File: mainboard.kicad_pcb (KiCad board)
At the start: 2 copper layers, 76.8 x 33.7 mm, 38 parts, among them J1 105017-1001, J2 Conn_01x04_Female, J3 Conn_01x02_Female, J4 Conn_01x09_Female, J5 Conn_01x02_Female, J6 Conn_01x02_Female, J7 Conn_01x04_Female, J8 Conn_01x03_Female, Q1 AOD4184A, U1 ESP32-WROOM-32E_(16MB)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

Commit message: h
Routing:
- net IRB: track 28.8 -> 30.6 mm
- net 3V3: track 129.9 -> 130.5 mm
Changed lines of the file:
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@@
-(kicad_pcb (version 20171130) (host pcbnew "(5.1.9)-1")
+(kicad_pcb (version 20171130) (host pcbnew "(5.1.9-0-10_14)")
   (general
     (thickness 1.6)
-    (drawings 29)
-    (tracks 313)
+    (drawings 31)
+    (tracks 316)
     (zones 0)
     (modules 38)
@@
   )
   (setup
-    (last_trace_width 0.25)
+    (last_trace_width 0.635)
     (user_trace_width 0.4)
     (user_trace_width 0.5)
@@
     )
   )
+  (dimension 33.655 (width 0.15) (layer Dwgs.User)
+    (gr_text "33.655 mm" (at 156.24 99.3775 90) (layer Dwgs.User)
+      (effects (font (size 1 1) (thickness 0.15)))
+    )
+    (feature1 (pts (xy 147.955 82.55) (xy 155.526421 82.55)))
+    (feature2 (pts (xy 147.955 116.205) (xy 155.526421 116.205)))
+    (crossbar (pts (xy 154.94 116.205) (xy 154.94 82.55)))
+    (arrow1a (pts (xy 154.94 82.55) (xy 155.526421 83.676504)))
+    (arrow1b (pts (xy 154.94 82.55) (xy 154.353579 83.676504)))
+    (arrow2a (pts (xy 154.94 116.205) (xy 155.526421 115.078496)))
+    (arrow2b (pts (xy 154.94 116.205) (xy 154.353579 115.078496)))
+  )
+  (dimension 76.835 (width 0.15) (layer Dwgs.User)
+    (gr_text "76.835 mm" (at 109.5375 125.76) (layer Dwgs.User)
+      (effects (font (size 1 1) (thickness 0.15)))
+    )
+    (feature1 (pts (xy 147.955 116.205) (xy 147.955 125.046421)))
+    (feature2 (pts (xy 71.12 116.205) (xy 71.12 125.046421)))
+    (crossbar (pts (xy 71.12 124.46) (xy 147.955 124.46)))
+    (arrow1a (pts (xy 147.955 124.46) (xy 146.828496 125.046421)))
+    (arrow1b (pts (xy 147.955 124.46) (xy 146.828496 123.873579)))
+    (arrow2a (pts (xy 71.12 124.46) (xy 72.246504 125.046421)))
+    (arrow2b (pts (xy 71.12 124.46) (xy 72.246504 123.873579)))
+  )
   (gr_line (start 139.065 82.55) (end 143.51 82.55) (layer Edge.Cuts) (width 0.05))
   (gr_text + (at 99.695 103.886) (layer F.SilkS)
@@
   (segment (start 127.476 103.124) (end 128.076 103.124) (width 0.635) (layer F.Cu) (net 14))
   (segment (start 129.032 109.22) (end 130.175 109.22) (width 0.635) (layer F.Cu) (net 14))
-  (segment (start 105.546 85.672) (end 107.897 85.672) (width 0.635) (layer F.Cu) (net 14))
   (segment (start 107.897 85.672) (end 107.897 85.672) (width 0.635) (layer F.Cu) (net 14))
   (segment (start 93.32 87.376) (end 88.29 87.376) (width 0.635) (layer F.Cu) (net 14))
@@
   (segment (start 135.219502 109.22) (end 137.759502 111.76) (width 0.635) (layer F.Cu) (net 14))
   (segment (start 130.175 109.22) (end 135.219502 109.22) (width 0.635) (layer F.Cu) (net 14))
-  (segment (start 107.897 85.672) (end 107.897 85.672) (width 0.635) (layer B.Cu) (net 14))
-  (via (at 107.897 85.672) (size 1.5) (drill 0.5) (layers F.Cu B.Cu) (net 14))
+  (via (at 109.22 85.725) (size 1.5) (drill 0.5) (layers F.Cu B.Cu) (net 14))
   (segment (start 88.274 87.36) (end 88.29 87.376) (width 0.635) (layer F.Cu) (net 14))
   (segment (start 85.36 89.535) (end 85.36 87.995) (width 0.635) (layer F.Cu) (net 14))
@@
   (segment (start 99.23 84.455) (end 99.23 87.73) (width 0.635) (layer F.Cu) (net 14))
   (segment (start 132.662 85.672) (end 132.715 85.725) (width 0.635) (layer B.Cu) (net 14))
-  (segment (start 107.897 85.672) (end 132.662 85.672) (width 0.635) (layer B.Cu) (net 14))
   (segment (start 135.89 85.725) (end 139.065 88.9) (width 0.635) (layer F.Cu) (net 14))
   (segment (start 132.715 85.725) (end 135.89 85.725) (width 0.635) (layer F.Cu) (net 14))
@@
   (segment (start 139.065 88.9) (end 141.605 91.44) (width 0.635) (layer F.Cu) (net 14))
   (segment (start 141.605 110.529098) (end 141.605 92.71) (width 0.635) (layer F.Cu) (net 14))
+  (segment (start 105.546 85.672) (end 108.638 85.672) (width 0.635) (layer F.Cu) (net 14))
+  (segment (start 108.691 85.725) (end 108.638 85.672) (width 0.635) (layer F.Cu) (net 14))
+  (segment (start 109.22 85.725) (end 108.691 85.725) (width 0.635) (layer F.Cu) (net 14))
+  (segment (start 109.22 85.725) (end 109.855 85.09) (width 0.635) (layer B.Cu) (net 14))
+  (segment (start 132.08 85.09) (end 132.715 85.725) (width 0.635) (layer B.Cu) (net 14))
+  (segment (start 109.855 85.09) (end 132.08 85.09) (width 0.635) (layer B.Cu) (net 14))
   (segment (start 123.825 111.744) (end 123.825 113.665) (width 0.635) (layer F.Cu) (net 15))
   (segment (start 132.08 112.395) (end 132.08 111.252) (width 0.635) (layer F.Cu) (net 15))
@@
   (segment (start 75.319 106.583) (end 72.944 106.583) (width 0.25) (layer F.Cu) (net 27))
   (segment (start 72.644 106.283) (end 72.644 108.783) (width 0.635) (layer F.Cu) (net 27))
-  (via (at 80.01 85.09) (size 1.5) (drill 0.5) (layers F.Cu B.Cu) (net 27))
+  (via (at 84.455 84.455) (size 1.5) (drill 0.5) (layers F.Cu B.Cu) (net 27))
   (segment (start 127.582 93.292) (end 122.546 93.292) (width 0.635) (layer F.Cu) (net 29))
   (segment (start 139.065 104.14) (end 138.43 104.14) (width 0.635) (layer F.Cu) (net 29))
@@
   (segment (start 123.264 100.912) (end 125.476 103.124) (width 0.635) (layer F.Cu) (net 37))
   (segment (start 122.546 100.912) (end 123.264 100.912) (width 0.635) (layer F.Cu) (net 37))
-  (segment (start 105.546 92.022) (end 107.368 92.022) (width 0.635) (layer F.Cu) (net 38))
-  (segment (start 107.368 92.022) (end 108.585 90.805) (width 0.635) (layer F.Cu) (net 38))
   (segment (start 108.585 90.805) (end 108.585 90.805) (width 0.635) (layer F.Cu) (net 38))
   (segment (start 107.315 92.075) (end 107.315 111.887) (width 0.635) (layer B.Cu) (net 38))
   (segment (start 107.315 111.887) (end 107.8865 112.4585) (width 0.635) (layer B.Cu) (net 38))
-  (segment (start 108.585 90.805) (end 107.315 92.075) (width 0.635) (layer B.Cu) (net 38))
   (segment (start 107.8865 112.4585) (end 109.474 114.046) (width 0.635) (layer B.Cu) (net 38))
   (segment (start 107.442 112.014) (end 107.8865 112.4585) (width 0.635) (layer B.Cu) (net 38))
-  (via (at 108.585 90.805) (size 1.5) (drill 0.5) (layers F.Cu B.Cu) (net 38))
+  (via (at 109.22 90.17) (size 1.5) (drill 0.5) (layers F.Cu B.Cu) (net 38))
+  (segment (start 107.315 92.075) (end 109.22 90.17) (width 0.635) (layer B.Cu) (net 38))
+  (segment (start 107.368 92.022) (end 105.546 92.022) (width 0.635) (layer F.Cu) (net 38))
+  (segment (start 109.22 90.17) (end 107.368 92.022) (width 0.635) (layer F.Cu) (net 38))
   (segment (start 122.546 90.752) (end 125.042 90.752) (width 0.635) (layer F.Cu) (net 42))
   (segment (start 125.042 90.752) (end 125.042 90.752) (width 0.635) (layer F.Cu) (net 42))

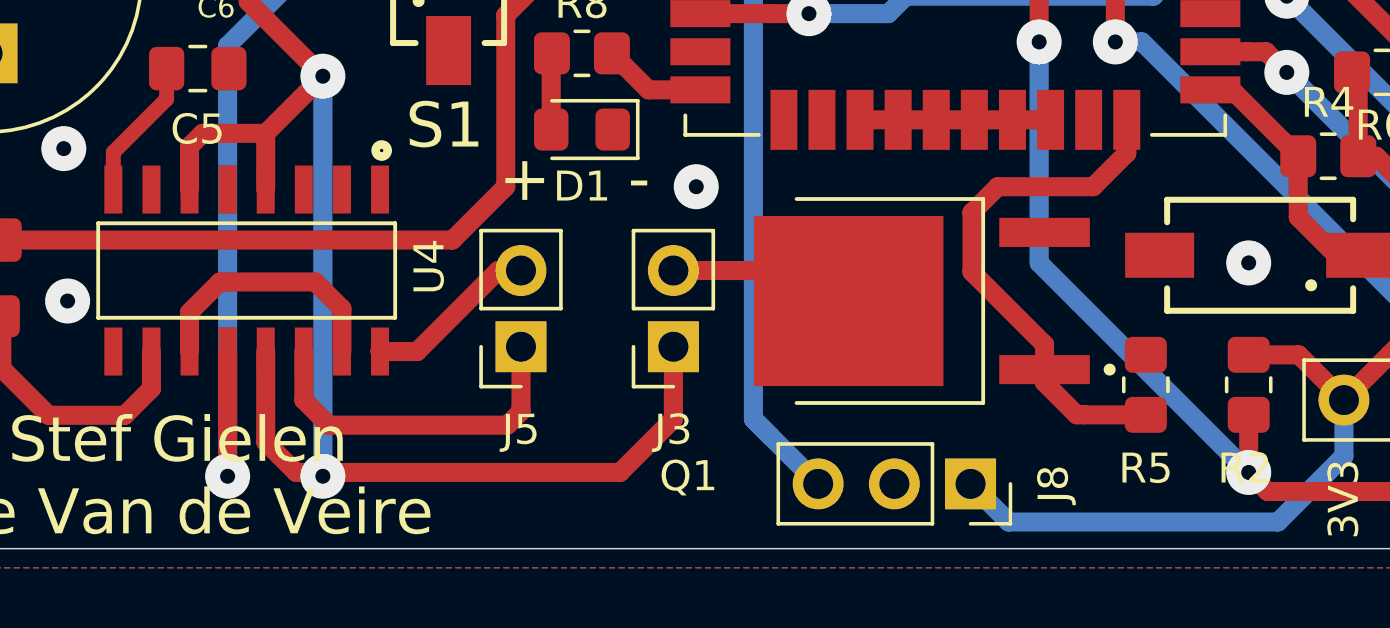
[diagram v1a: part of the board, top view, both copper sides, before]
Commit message: fixes
-pullup aan IRB
-mute aan 5V
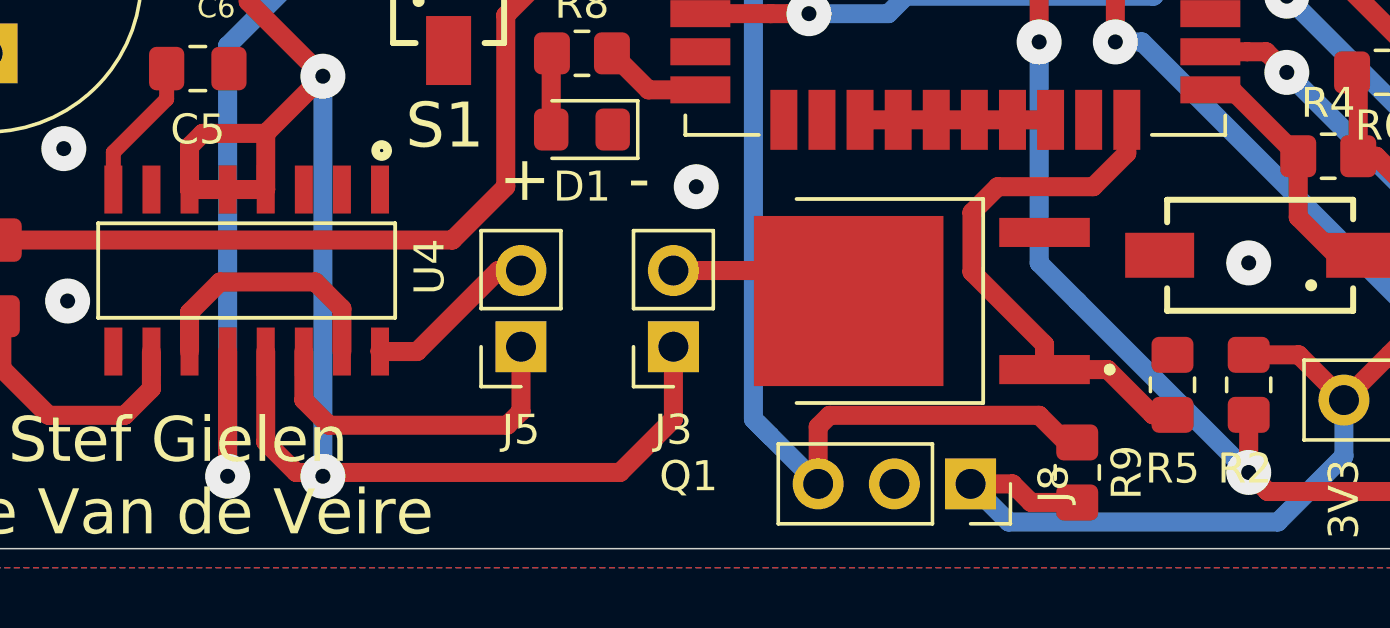
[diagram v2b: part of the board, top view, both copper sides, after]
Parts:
- added R9: 10K, Resistor_SMD:R_0805_2012Metric_Pad1.20x1.40mm_HandSolder, F.Cu at (118.1, 113.7)
- moved R5 0.89 mm to (121.3, 110.7)
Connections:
- S3 pad : GND -> (no net)
- U4 pad 5: Net-(U4-Pad5) -> 5V
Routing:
- net IRB: track 30.6 -> 41.7 mm
- net 3V3: track 130.5 -> 134.3 mm
- net 5V: track 82.5 -> 85.1 mm
- net Mosfet_Trig: track 17.6 -> 18.2 mm

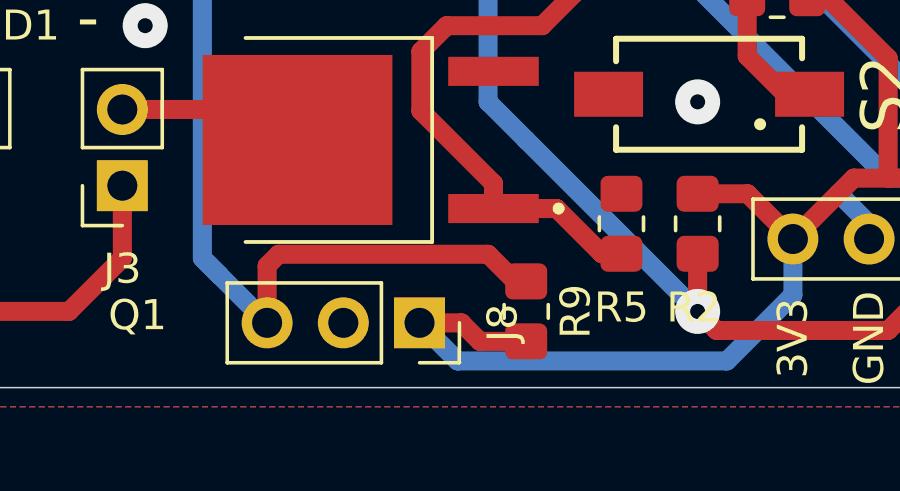
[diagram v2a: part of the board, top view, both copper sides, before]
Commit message: fixes
10k pullup
mute aan 5V
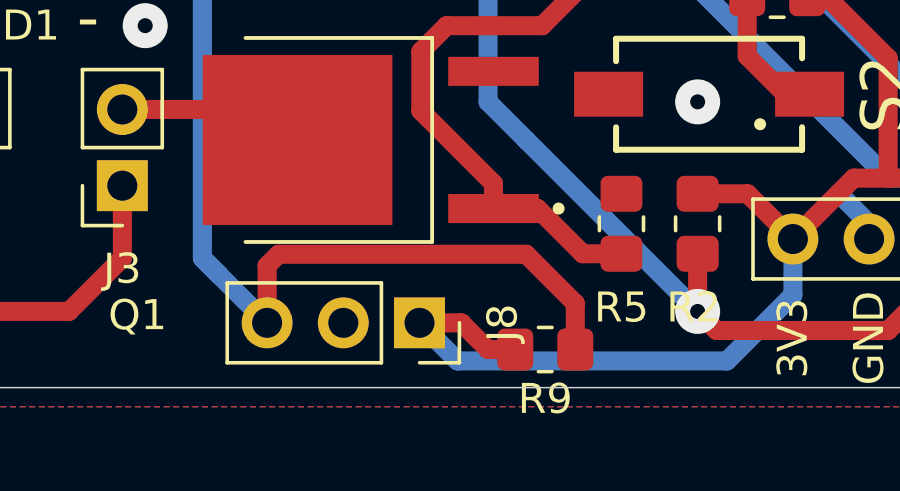
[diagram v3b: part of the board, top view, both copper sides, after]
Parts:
- moved R9 1.42 mm to (118.7, 114.9), turned to 180 degrees
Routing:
- net IRB: track 41.7 -> 45.2 mm

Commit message: diode opgezwierd
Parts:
- added D2: D, Diode_SMD:D_0805_2012Metric_Pad1.15x1.40mm_HandSolder, F.Cu at (101.6, 108.0)
- moved J5 1.14 mm to (98.4, 109.5)
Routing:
- net 5V: track 85.1 -> 88.3 mm
- net Mosfet_Out-: track 6.78 -> 9.84 mm
- net -OUT_R: track 11.6 -> 10.1 mm
- net +OUT_R: track 5.85 -> 5.08 mm
- net INR: track 30.2 -> 29.5 mm

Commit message: Revert "diode opgezwierd"
This reverts commit 37b3bf43883e8e94795329db478c9cb5caa1757c.
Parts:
- removed D2: D, Diode_SMD:D_0805_2012Metric_Pad1.15x1.40mm_HandSolder
- moved J5 1.14 mm to (99.6, 109.5)
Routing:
- net 5V: track 88.3 -> 85.1 mm
- net Mosfet_Out-: track 9.84 -> 6.78 mm
- net -OUT_R: track 10.1 -> 11.6 mm
- net +OUT_R: track 5.08 -> 5.85 mm
- net INR: track 29.5 -> 30.2 mm

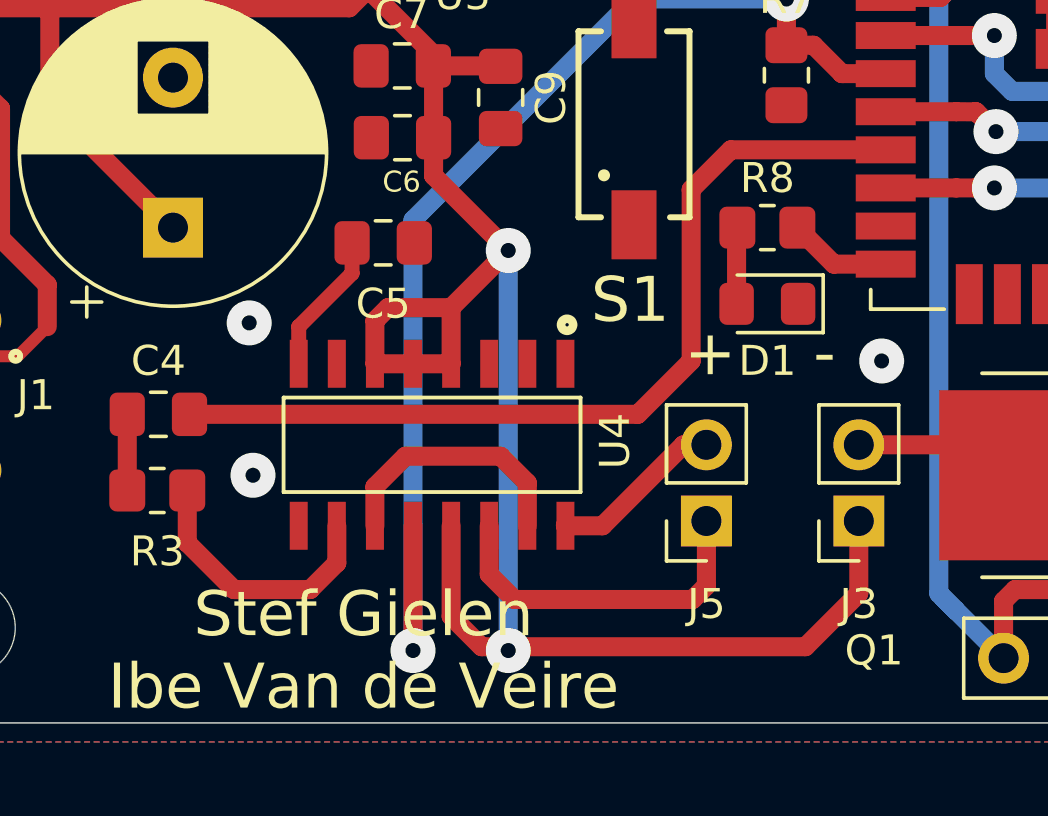
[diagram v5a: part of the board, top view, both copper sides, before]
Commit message: amai ik ben er een boeltje van aan het maken
flyback diode toegevoegd
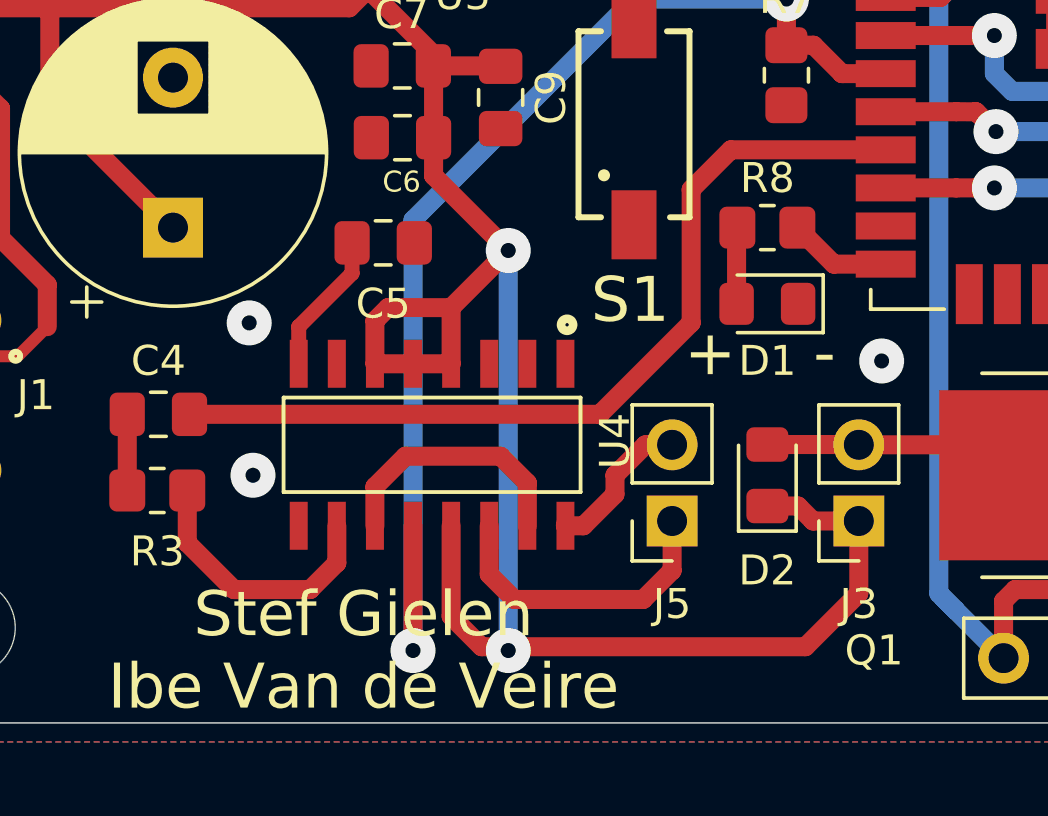
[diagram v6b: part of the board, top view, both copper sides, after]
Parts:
- added D2: D, Diode_SMD:D_0805_2012Metric_Pad1.15x1.40mm_HandSolder, F.Cu at (101.6, 108.0)
- moved J5 1.14 mm to (98.4, 109.5)
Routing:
- net 5V: track 85.1 -> 88.3 mm
- net Mosfet_Out-: track 6.78 -> 9.84 mm
- net -OUT_R: track 11.6 -> 10.1 mm
- net +OUT_R: track 5.85 -> 5.08 mm
- net INR: track 30.2 -> 29.5 mm
